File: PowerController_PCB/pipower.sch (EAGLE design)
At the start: 25 parts, among them IC1 12F629, Q1 AP4435GH, Q2 AP4435GH, T1 BC848, T2 BC848, T3 BC848, X1 22-23-2021, X2 22-23-2021

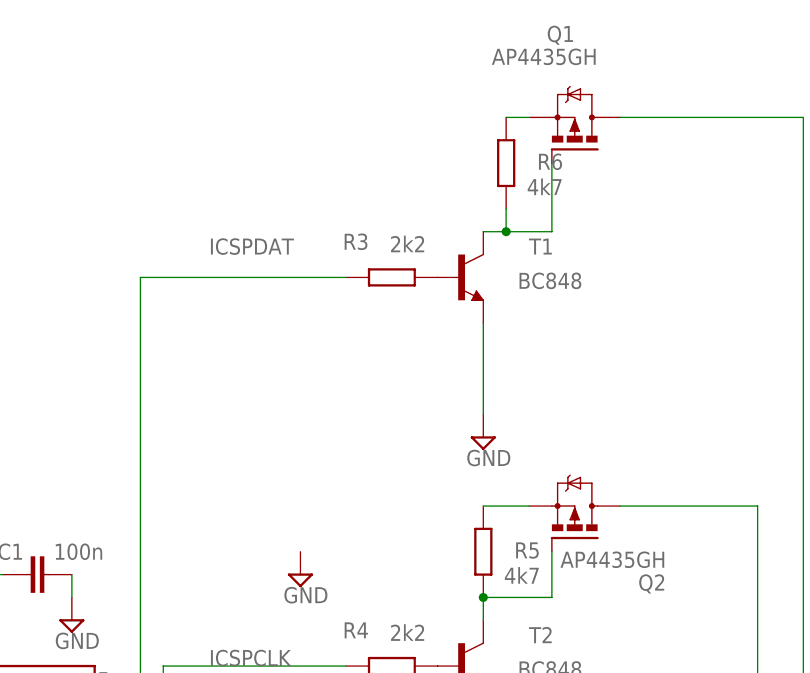
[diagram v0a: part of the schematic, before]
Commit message: Added files via upload
faltaba una pista
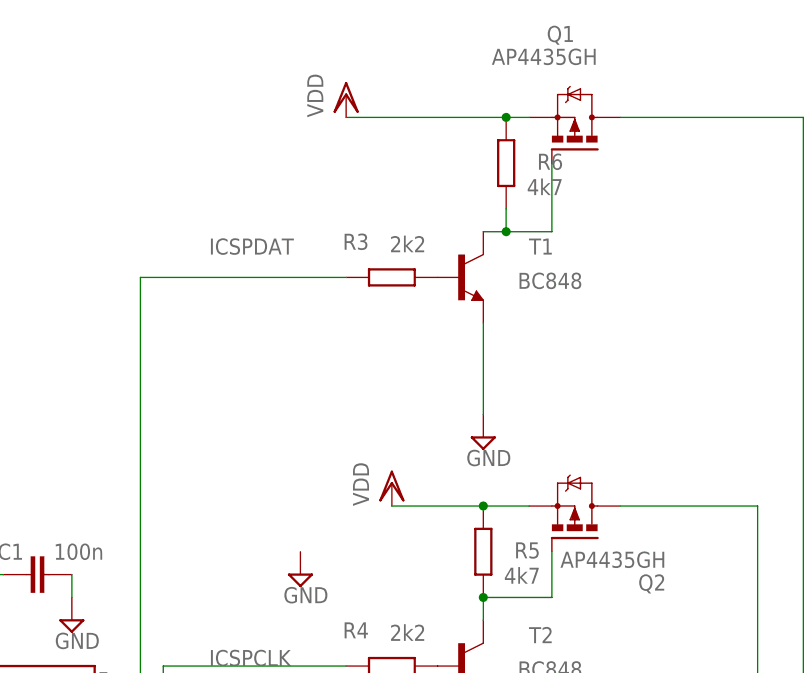
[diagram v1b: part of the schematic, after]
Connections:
- removed net N$12: Q1.S, R6.2
- removed net N$4: Q2.S, R5.2
- net VDD: now also Q1.S, Q2.S, R5.2, R6.2
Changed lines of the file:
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@@
 <part name="SJ1" library="jumper" deviceset="SJ" device=""/>
 <part name="JP1" library="daspilker" deviceset="USB-RECEPTABLE" device=""/>
+<part name="VDD6" library="supply1" deviceset="VDD" device=""/>
+<part name="VDD7" library="supply1" deviceset="VDD" device=""/>
 </parts>
 <sheets>
@@
 <instance part="SJ1" gate="1" x="15.24" y="63.5"/>
 <instance part="JP1" gate="G$1" x="-15.24" y="15.24" rot="MR0"/>
+<instance part="VDD6" gate="G$1" x="86.36" y="142.24"/>
+<instance part="VDD7" gate="G$1" x="91.44" y="99.06"/>
 </instances>
 <busses>
@@
 <wire x1="0" y1="63.5" x2="0" y2="66.04" width="0.1524" layer="91"/>
 </segment>
+<segment>
+<pinref part="Q1" gate="G$1" pin="S"/>
+<pinref part="R6" gate="G$1" pin="2"/>
+<wire x1="106.68" y1="139.7" x2="104.14" y2="139.7" width="0.1524" layer="91"/>
+<wire x1="104.14" y1="139.7" x2="86.36" y2="139.7" width="0.1524" layer="91"/>
+<junction x="104.14" y="139.7"/>
+<pinref part="VDD6" gate="G$1" pin="VDD"/>
+</segment>
+<segment>
+<pinref part="Q2" gate="G$1" pin="S"/>
+<pinref part="R5" gate="G$1" pin="2"/>
+<wire x1="106.68" y1="96.52" x2="101.6" y2="96.52" width="0.1524" layer="91"/>
+<wire x1="101.6" y1="96.52" x2="91.44" y2="96.52" width="0.1524" layer="91"/>
+<junction x="101.6" y="96.52"/>
+<pinref part="VDD7" gate="G$1" pin="VDD"/>
+</segment>
 </net>
 <net name="N$10" class="0">
@@
 </segment>
 </net>
-<net name="N$4" class="0">
-<segment>
-<pinref part="Q2" gate="G$1" pin="S"/>
-<pinref part="R5" gate="G$1" pin="2"/>
-<wire x1="106.68" y1="96.52" x2="101.6" y2="96.52" width="0.1524" layer="91"/>
-</segment>
-</net>
 <net name="N$8" class="0">
 <segment>
@@
 </segment>
 </net>
-<net name="N$12" class="0">
-<segment>
-<pinref part="Q1" gate="G$1" pin="S"/>
-<pinref part="R6" gate="G$1" pin="2"/>
-<wire x1="106.68" y1="139.7" x2="104.14" y2="139.7" width="0.1524" layer="91"/>
-</segment>
-</net>
